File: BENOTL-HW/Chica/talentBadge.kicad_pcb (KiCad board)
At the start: 2 copper layers, 62 parts, among them P1 USB_A, P2 OLED, P3 Batt, P4 PS, P5 sd_card_spi, Q1 MMBT3904, Q2 MMBT3904, Q3 IR phototransistor, SW1 B1, SW2 B2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

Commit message: Archivos Layout para PCB Chica
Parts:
- added svg2mod: G***, Chica:Chica_Contorno, F.Cu at (74.4, 111.0)
- added svg2mod: G***, Chica:Chica_SilkS_1, F.Cu at (73.2, 111.0)
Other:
- board outline added: 96.6 x 102.2 mm

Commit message: Cambios Archivos Layout PCB Chica
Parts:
- removed C1, C3, C4, C5: 4.7uF, Capacitors_SMD:C_0805_HandSoldering
- removed C10, C11, C12, C13, C14, C15, C16, C17, C18, C2, C6, C7, C8, C9: 0.1uF, Capacitors_SMD:C_0805_HandSoldering
- removed D1: LED, LEDs:LED_D3.0mm
- removed D2: Diode, Diodes_SMD:D_SMA
- removed F1: Fuse_Small, talentBadge:0440.500WRA
- removed P1: USB_A, talentBadge:629105150921
- removed P2: OLED, Pin_Headers:Pin_Header_Straight_1x04_Pitch2.54mm
- removed P3: Batt, Pin_Headers:Pin_Header_Straight_1x02_Pitch2.54mm
- removed P4: PS, Pin_Headers:Pin_Header_Straight_1x02_Pitch2.54mm
- removed P5: sd_card_spi, talentBadge:MOLEX_0475710001
- removed Q1, Q2: MMBT3904, TO_SOT_Packages_SMD:SOT-23
- removed Q3: IR phototransistor, LEDs:LED_D5.0mm
- removed R1, R10, R11, R12, R13, R14, R4, R5, R6, R7, R8: 10k, Resistors_SMD:R_0805_HandSoldering
- removed R2: 470, Resistors_SMD:R_0805_HandSoldering
- removed R3: 1k, Resistors_SMD:R_0805_HandSoldering
- removed R9: 100, Resistors_SMD:R_0805_HandSoldering
- removed SW1: B1, talentBadge:SW_TL3342F160QG
- removed SW2: B2, talentBadge:SW_TL3342F160QG
- removed SW3: RST, talentBadge:SW_TL3342F160QG
- removed U1: esp8266-12, talentBadge:ESP-12E_SMD
- removed U10, U11, U12, U13, U14, U15, U16, U5, U6, U7, U8, U9: ws2812b, LEDs:LED_WS2812B-PLCC4
- removed U2: CP2102N, talentBadge:QFN-24-5x5mm_Pitch0.50mm
- removed U3: SP0503BAHTG, talentBadge:SOT143
- removed U4: AP111733, TO_SOT_Packages_SMD:SOT-223
- removed the svg2mod at (73.2, 111.0)
- added svg2mod: G***, Chica:Chica_Silks_Sin_antena_Mask, F.Cu at (72.5, 111.2)

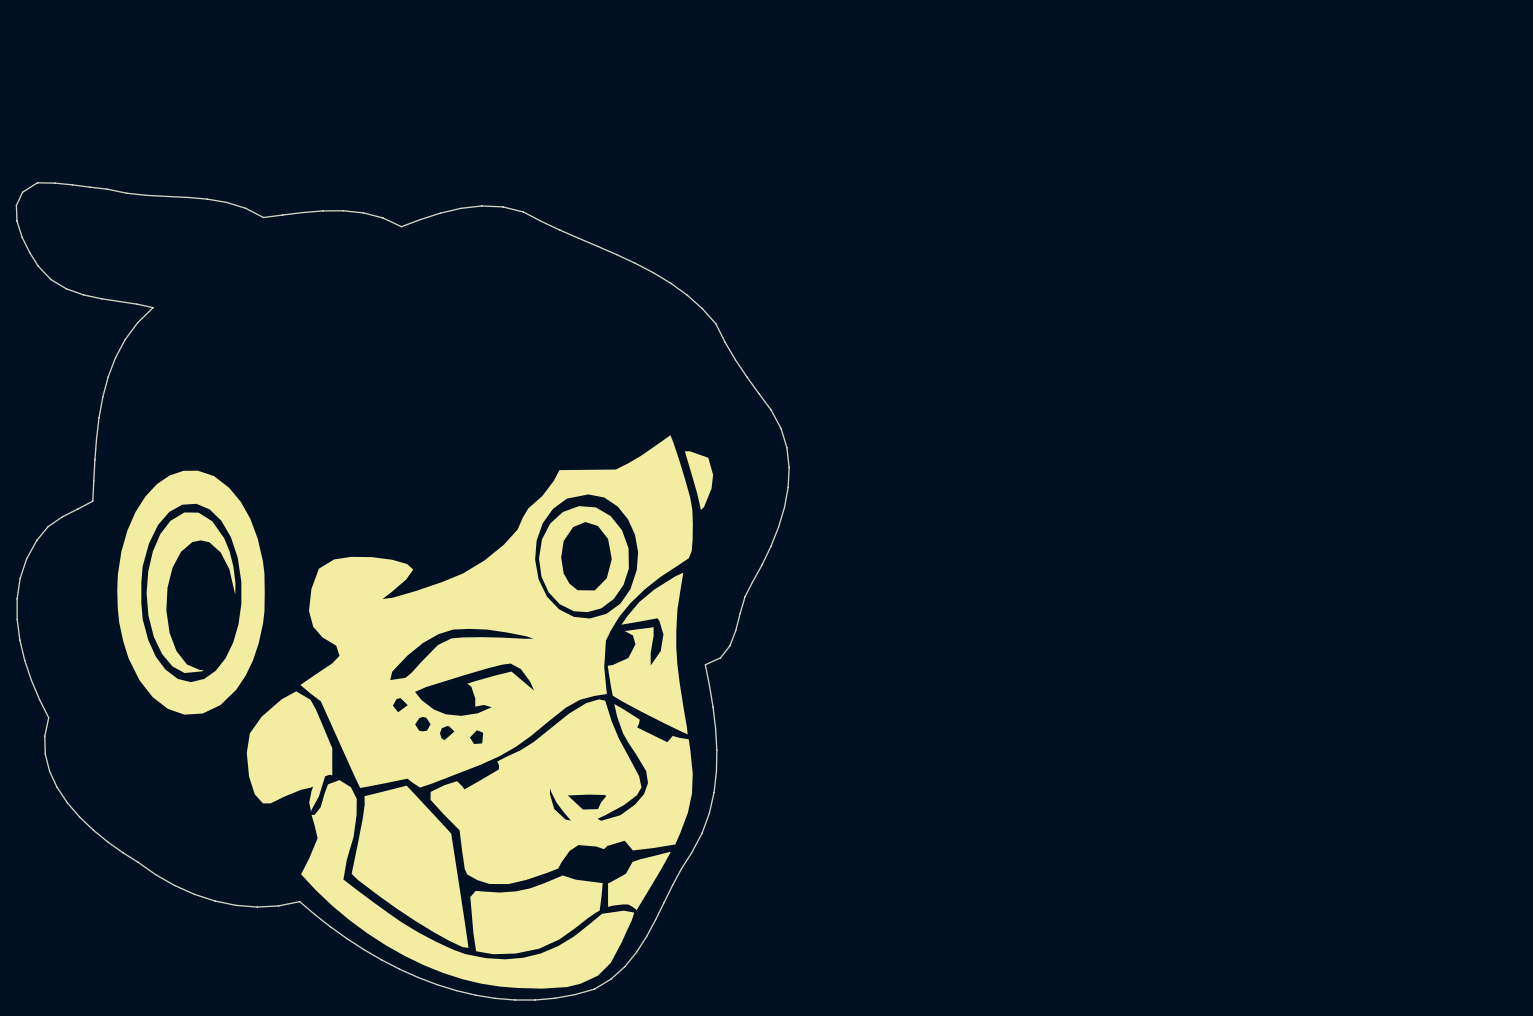
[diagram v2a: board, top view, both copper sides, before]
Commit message: Routeo y layout de chica - incompleto.
Tuve que cambiar el grid del schematico por que en la seccion del esp estabamovido.
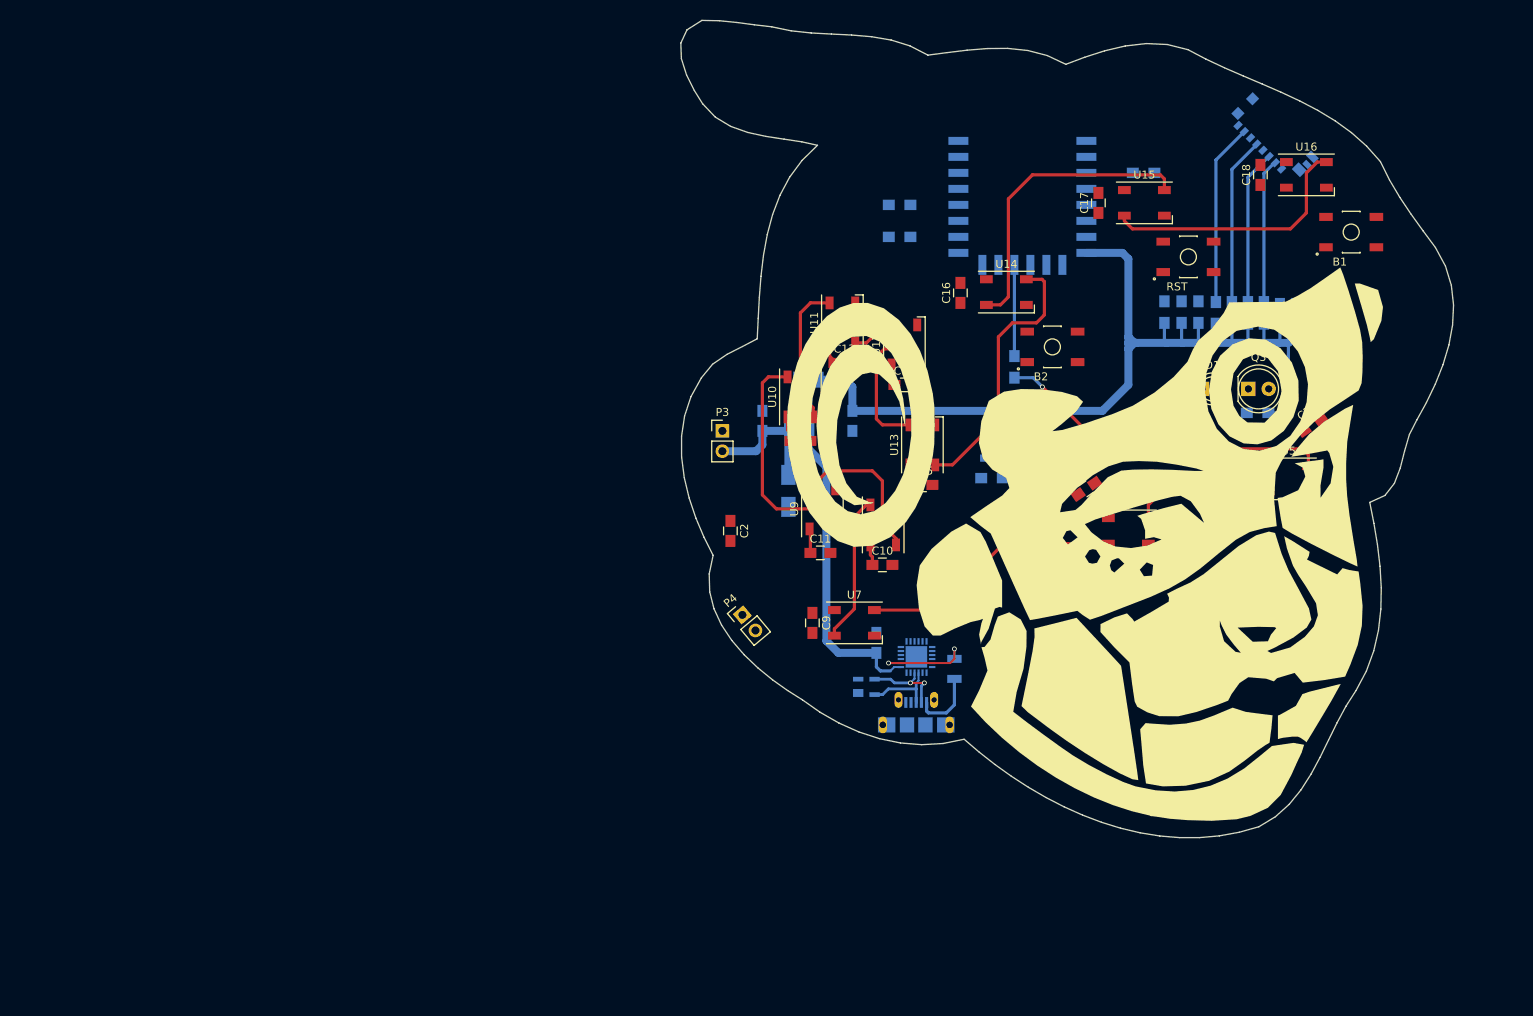
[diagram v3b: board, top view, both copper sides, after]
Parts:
- removed the svg2mod at (74.4, 111.0)
- removed the svg2mod at (72.5, 111.2)
- added C1: 4.7uF, Capacitors_SMD:C_0805_HandSoldering, B.Cu at (134.2, 117.0)
- added C10: 0.1uF, Capacitors_SMD:C_0805_HandSoldering, F.Cu at (135.0, 107.2)
- added C11: 0.1uF, Capacitors_SMD:C_0805_HandSoldering, F.Cu at (127.2, 105.8)
- added C12: 0.1uF, Capacitors_SMD:C_0805_HandSoldering, F.Cu at (124.8, 91.8)
- added C13: 0.1uF, Capacitors_SMD:C_0805_HandSoldering, F.Cu at (130.2, 82.0)
- added C14: 0.1uF, Capacitors_SMD:C_0805_HandSoldering, F.Cu at (137.8, 84.8)
- added C15: 0.1uF, Capacitors_SMD:C_0805_HandSoldering, F.Cu at (140.0, 97.2)
- added C16: 0.1uF, Capacitors_SMD:C_0805_HandSoldering, F.Cu at (144.8, 73.2)
- added C17: 0.1uF, Capacitors_SMD:C_0805_HandSoldering, F.Cu at (162.0, 62.0)
- added C18: 0.1uF, Capacitors_SMD:C_0805_HandSoldering, F.Cu at (182.2, 58.5)
- added C2: 0.1uF, Capacitors_SMD:C_0805_HandSoldering, F.Cu at (116.0, 103.0)
- added C3: 4.7uF, Capacitors_SMD:C_0805_HandSoldering, B.Cu at (120.0, 89.2)
- added C4: 4.7uF, Capacitors_SMD:C_0805_HandSoldering, B.Cu at (131.2, 89.2)
- added C5: 4.7uF, Capacitors_SMD:C_0805_HandSoldering, B.Cu at (186.7, 75.9)
- added C6: 0.1uF, Capacitors_SMD:C_0805_HandSoldering, B.Cu at (184.7, 75.9)
- added C7: 0.1uF, Capacitors_SMD:C_0805_HandSoldering, F.Cu at (188.8, 89.8)
- added C8: 0.1uF, Capacitors_SMD:C_0805_HandSoldering, F.Cu at (160.5, 97.8)
- added C9: 0.1uF, Capacitors_SMD:C_0805_HandSoldering, F.Cu at (126.2, 114.5)
- added D1: LED, LEDs:LED_D3.0mm, F.Cu at (175.0, 85.2)
- added D2: Diode, Diodes_SMD:D_SMA, B.Cu at (123.2, 98.0)
- added F1: Fuse_Small, talentBadge:0440.500WRA, B.Cu at (144.0, 121.5)
- added P1: USB_A, talentBadge:629105150921, B.Cu at (139.3, 127.1)
- added P2: OLED, Pin_Headers:Pin_Header_Straight_1x04_Pitch2.54mm, F.Cu at (177.5, 137.2)
- added P3: Batt, Pin_Headers:Pin_Header_Straight_1x02_Pitch2.54mm, F.Cu at (115.0, 90.5)
- added P4: PS, Pin_Headers:Pin_Header_Straight_1x02_Pitch2.54mm, F.Cu at (117.5, 113.5)
- added P5: sd_card_spi, talentBadge:MOLEX_0475710001, B.Cu at (183.4, 54.3)
- added Q1: MMBT3904, TO_SOT_Packages_SMD:SOT-23, B.Cu at (155.1, 92.9)
- added Q2: MMBT3904, TO_SOT_Packages_SMD:SOT-23, B.Cu at (148.6, 92.9)
- added Q3: IR phototransistor, LEDs:LED_D5.0mm, F.Cu at (180.8, 85.2)
- added R1: 10k, Resistors_SMD:R_0805_HandSoldering, B.Cu at (167.7, 58.2)
- added R10: 10k, Resistors_SMD:R_0805_HandSoldering, B.Cu at (182.7, 75.7)
- added R11: 10k, Resistors_SMD:R_0805_HandSoldering, B.Cu at (180.7, 75.7)
- added R12: 10k, Resistors_SMD:R_0805_HandSoldering, B.Cu at (178.7, 75.7)
- added R13: 10k, Resistors_SMD:R_0805_HandSoldering, B.Cu at (176.7, 75.7)
- added R14: 10k, Resistors_SMD:R_0805_HandSoldering, B.Cu at (181.9, 88.2)
- added R15: 10K, Resistors_SMD:R_0805_HandSoldering, B.Cu at (137.2, 62.2)
- added R2: 470, Resistors_SMD:R_0805_HandSoldering, B.Cu at (151.5, 82.5)
- added R3: 1k, Resistors_SMD:R_0805_HandSoldering, B.Cu at (137.2, 66.2)
- added R4: 10k, Resistors_SMD:R_0805_HandSoldering, B.Cu at (155.1, 96.4)
- added R5: 10k, Resistors_SMD:R_0805_HandSoldering, B.Cu at (148.7, 96.4)
- added R6: 10k, Resistors_SMD:R_0805_HandSoldering, B.Cu at (170.2, 75.7)
- added R7: 10k, Resistors_SMD:R_0805_HandSoldering, B.Cu at (172.4, 75.7)
- added R8: 10k, Resistors_SMD:R_0805_HandSoldering, B.Cu at (174.5, 75.7)
- added R9: 100, Resistors_SMD:R_0805_HandSoldering, B.Cu at (176.1, 88.2)
- added SW1: B1, talentBadge:SW_TL3342F160QG, F.Cu at (193.6, 65.7)
- added SW2: B2, talentBadge:SW_TL3342F160QG, F.Cu at (156.2, 80.0)
- added SW3: RST, talentBadge:SW_TL3342F160QG, F.Cu at (173.2, 68.8)
- added U1: esp8266-12, footprints:esp8266-12, B.Cu at (152.5, 69.8)
- added U10: ws2812b, LEDs:LED_WS2812B-PLCC4, F.Cu at (124.8, 86.2)
- added U11: ws2812b, LEDs:LED_WS2812B-PLCC4, F.Cu at (130.0, 77.0)
- added U12: ws2812b, LEDs:LED_WS2812B-PLCC4, F.Cu at (137.8, 79.8)
- added U13: ws2812b, LEDs:LED_WS2812B-PLCC4, F.Cu at (140.0, 92.2)
- added U14: ws2812b, LEDs:LED_WS2812B-PLCC4, F.Cu at (150.5, 73.2)
- added U15: ws2812b, LEDs:LED_WS2812B-PLCC4, F.Cu at (167.8, 62.0)
- added U16: ws2812b, LEDs:LED_WS2812B-PLCC4, F.Cu at (188.0, 58.5)
- added U2: CP2102N, talentBadge:QFN-24-5x5mm_Pitch0.50mm, B.Cu at (139.3, 118.8)
- added U3: SP0503BAHTG, talentBadge:SOT143, B.Cu at (133.0, 122.5)
- added U4: AP111733, TO_SOT_Packages_SMD:SOT-223, B.Cu at (125.8, 87.2)
- added U5: ws2812b, LEDs:LED_WS2812B-PLCC4, F.Cu at (185.8, 96.5)
- added U6: ws2812b, LEDs:LED_WS2812B-PLCC4, F.Cu at (165.8, 103.0)
- added U7: ws2812b, LEDs:LED_WS2812B-PLCC4, F.Cu at (131.5, 114.5)
- added U8: ws2812b, LEDs:LED_WS2812B-PLCC4, F.Cu at (135.1, 102.2)
- added U9: ws2812b, LEDs:LED_WS2812B-PLCC4, F.Cu at (127.5, 100.2)
- added svg2mod: G***, talentBadge:Chica_Silks_Sin_antena_Mask, F.Cu at (156.2, 90.2)
- added svg2mod: G***, talentBadge:Chica_Contorno, F.Cu at (157.5, 90.8)
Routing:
- net +3V3: track 0.00 -> 184.4 mm
- net np: track 0.00 -> 42.1 mm, vias 0 -> 1
- net Net-(U14-Pad2): track 0.00 -> 37.8 mm
- net Net-(U13-Pad2): track 0.00 -> 33.9 mm
- net Net-(U15-Pad2): track 0.00 -> 32.7 mm
- net Net-(U6-Pad2): track 0.00 -> 32.7 mm
- net Net-(U10-Pad4): track 0.00 -> 29.0 mm
- net MISO: track 0.00 -> 22.8 mm
- net CLK: track 0.00 -> 21.0 mm
- net MOSI: track 0.00 -> 19.3 mm
- net np1: track 0.00 -> 19.3 mm
- net np2: track 0.00 -> 18.8 mm
- net Net-(U7-Pad2): track 0.00 -> 18.5 mm
- net CS: track 0.00 -> 18.1 mm
- net Net-(U10-Pad2): track 0.00 -> 17.8 mm
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
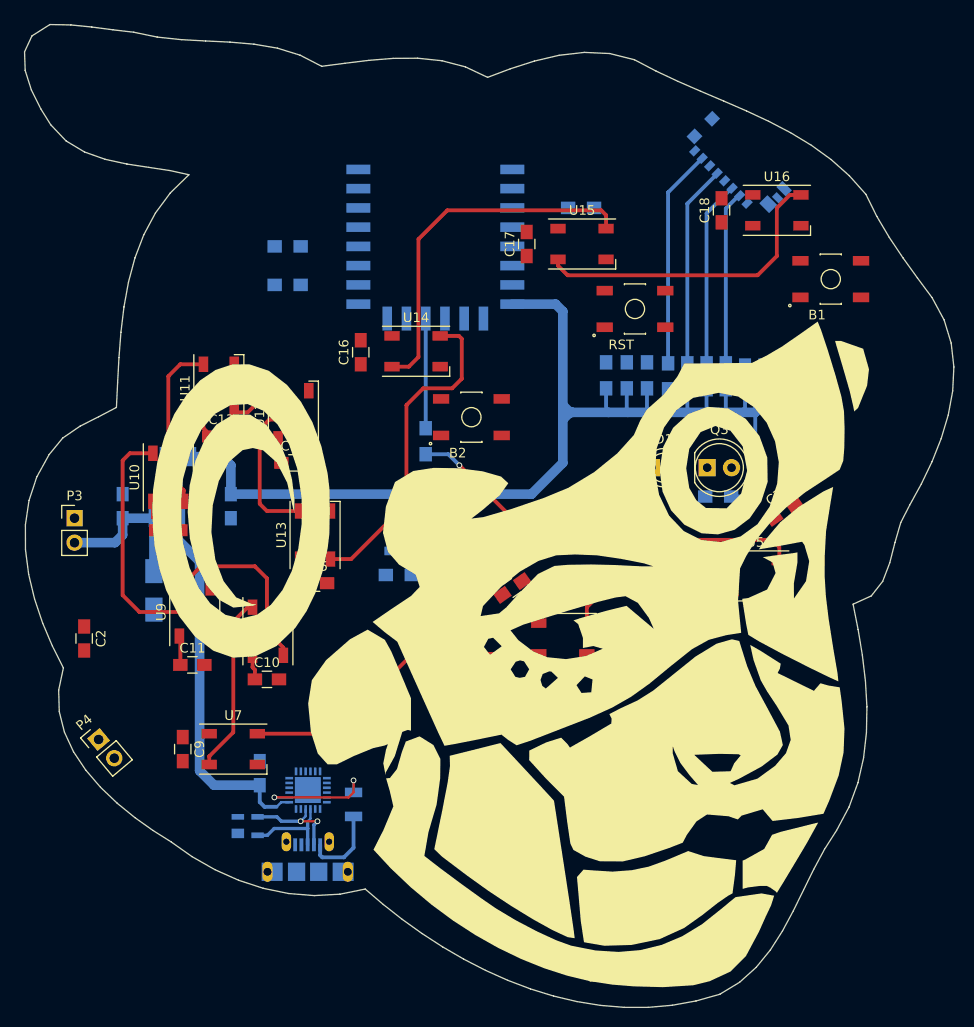
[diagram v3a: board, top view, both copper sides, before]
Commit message: Routeo Chica completo
Se cambio pin vcc y gnd en conector oled de posicion ya que estaban al reves.
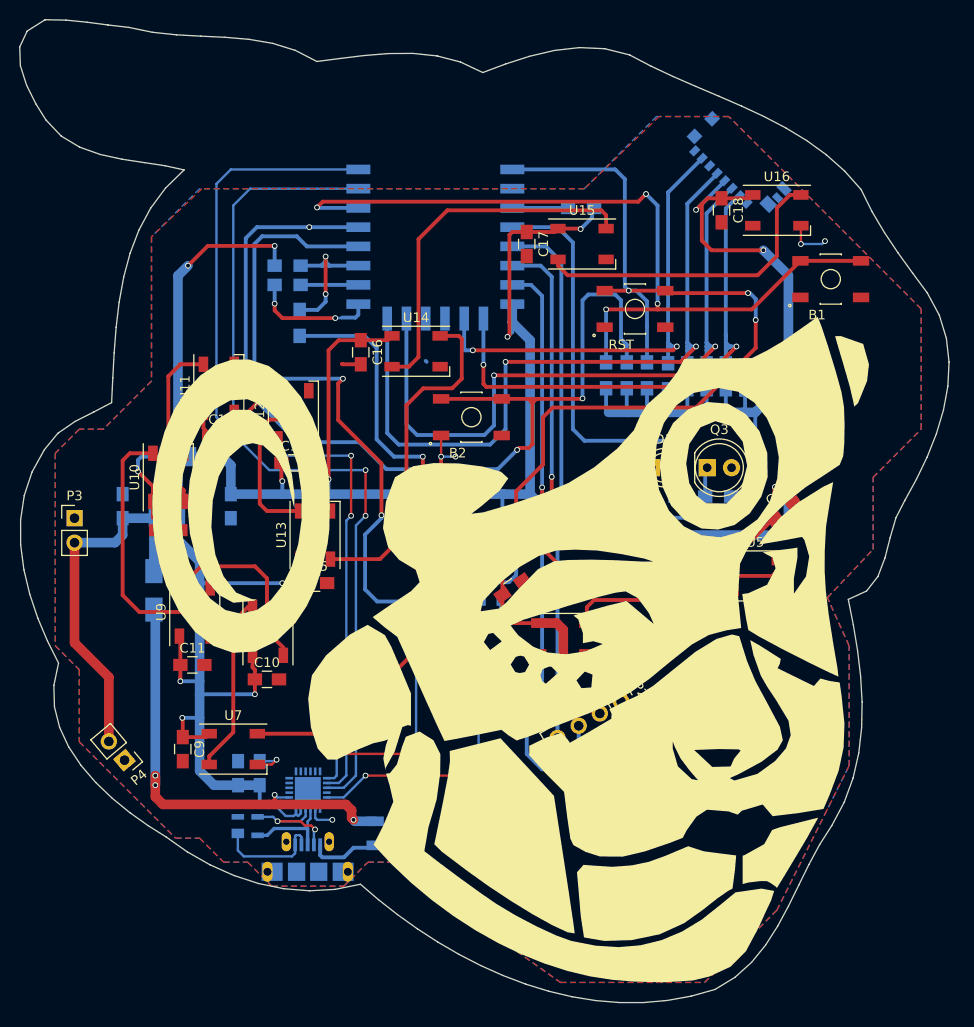
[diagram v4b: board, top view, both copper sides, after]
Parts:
- C2: moved to B.Cu
- moved P2 28.3 mm to (171.8, 109.5), turned to 300 degrees
- moved C2 21.3 mm to (132.0, 117.0), turned to 90 degrees
- moved R2 18.0 mm to (138.4, 70.2)
- moved Q1 6.17 mm to (158.3, 98.2)
- moved Q2 6.17 mm to (151.8, 98.2)
- moved R4 6.17 mm to (158.3, 101.7)
- moved R5 6.17 mm to (152.0, 101.7)
- moved F1 3.75 mm to (146.2, 124.5)
- moved P4 3.45 mm to (120.2, 115.7), turned to 220 degrees
- moved R15 2.00 mm to (137.2, 64.2)
- moved svg2mod 0.71 mm to (157.0, 90.2)
- moved svg2mod 0.50 mm to (156.2, 89.8)
- turned C16 to 270 degrees
- turned C17 to 270 degrees
- turned C18 to 270 degrees
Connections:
- P2 pad 1: +3V3 -> GND
- P2 pad 2: GND -> +3V3
- R2 pad 2: Net-(R2-Pad2) -> /GPIO2
- U1 pad 12: Net-(R2-Pad2) -> Net-(U1-Pad12)
- U1 pad 7: Net-(U1-Pad7) -> SCL
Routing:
- net +3V3: track 184.4 -> 422.2 mm, vias 0 -> 16
- net B2: track 0.00 -> 104.1 mm, vias 0 -> 3
- net RST: track 0.00 -> 99.3 mm, vias 0 -> 4
- net TXD: track 0.00 -> 93.1 mm, vias 0 -> 2
- net B1: track 0.00 -> 85.7 mm, vias 0 -> 4
- net RXD: track 0.00 -> 84.7 mm, vias 0 -> 2
- net GND: track 0.00 -> 66.7 mm, vias 0 -> 13
- net GPIO0: track 0.00 -> 65.2 mm, vias 0 -> 2
- net SCL: track 0.00 -> 61.7 mm, vias 0 -> 2
- net CLK: track 21.0 -> 75.8 mm, vias 0 -> 2
- net SDA: track 0.00 -> 52.8 mm, vias 0 -> 2
- net MOSI: track 19.3 -> 71.7 mm, vias 0 -> 2
- net IRT: track 0.00 -> 50.8 mm
- net IRL: track 0.00 -> 39.8 mm
- net RTS: track 0.00 -> 38.1 mm, vias 0 -> 4
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- added copper zone on B.Cu, net GND
- added copper zone on F.Cu, net GND

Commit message: Agregados logos chica
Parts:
- added G***: LOGO, talentBadge:pcbway_logo, B.Cu at (181.4, 97.0)
- added G***: LOGO, talentBadge:makers_logo, B.Cu at (151.1, 83.6)
- added G***: LOGO, talentBadge:wurth_logo, B.Cu at (182.9, 104.9)
- added G***: LOGO, talentBadge:espressif_logo, B.Cu at (182.9, 117.9)

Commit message: Agregado fix logo makers
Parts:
- moved G*** 3.59 mm to (154.7, 83.1)
